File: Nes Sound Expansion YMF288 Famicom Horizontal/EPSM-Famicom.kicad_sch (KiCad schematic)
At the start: 67 parts, among them J1 CARTRIDGE_F, J2 CONSOLE_M, J3 AudioJack4_SwitchTR1, U1 74HC688, U10 74HC132, U11 74HC257, U12 74HC257, U13 LM358, U14 74LVC1G373, U15 74HC257, U2 74HC139, U3 74HC174, U4 74HC174, U5 74HC688, U6 74HC688, U7 74HC132, U8 YMF288, U9 BU9480F, X1 SG-8002CA

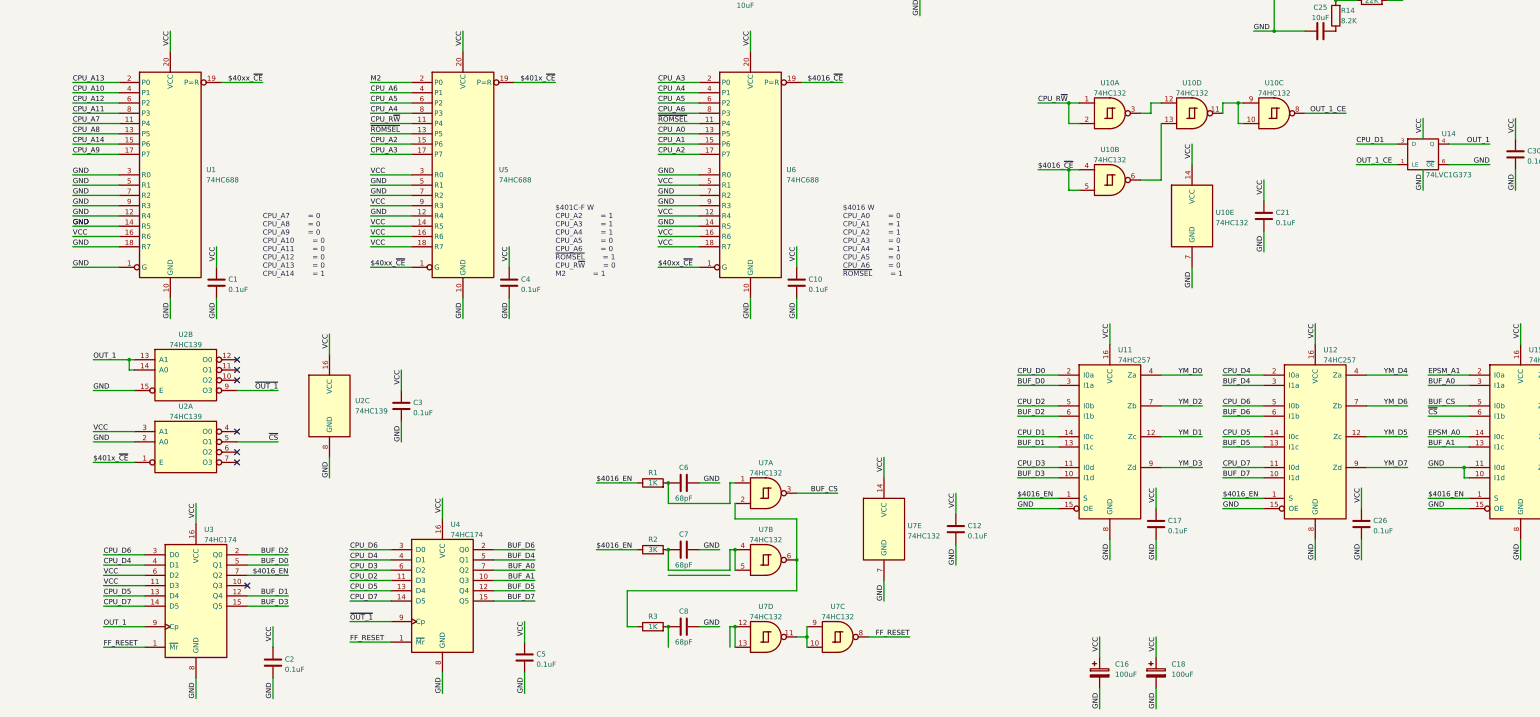
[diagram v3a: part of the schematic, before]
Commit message: Improved routing
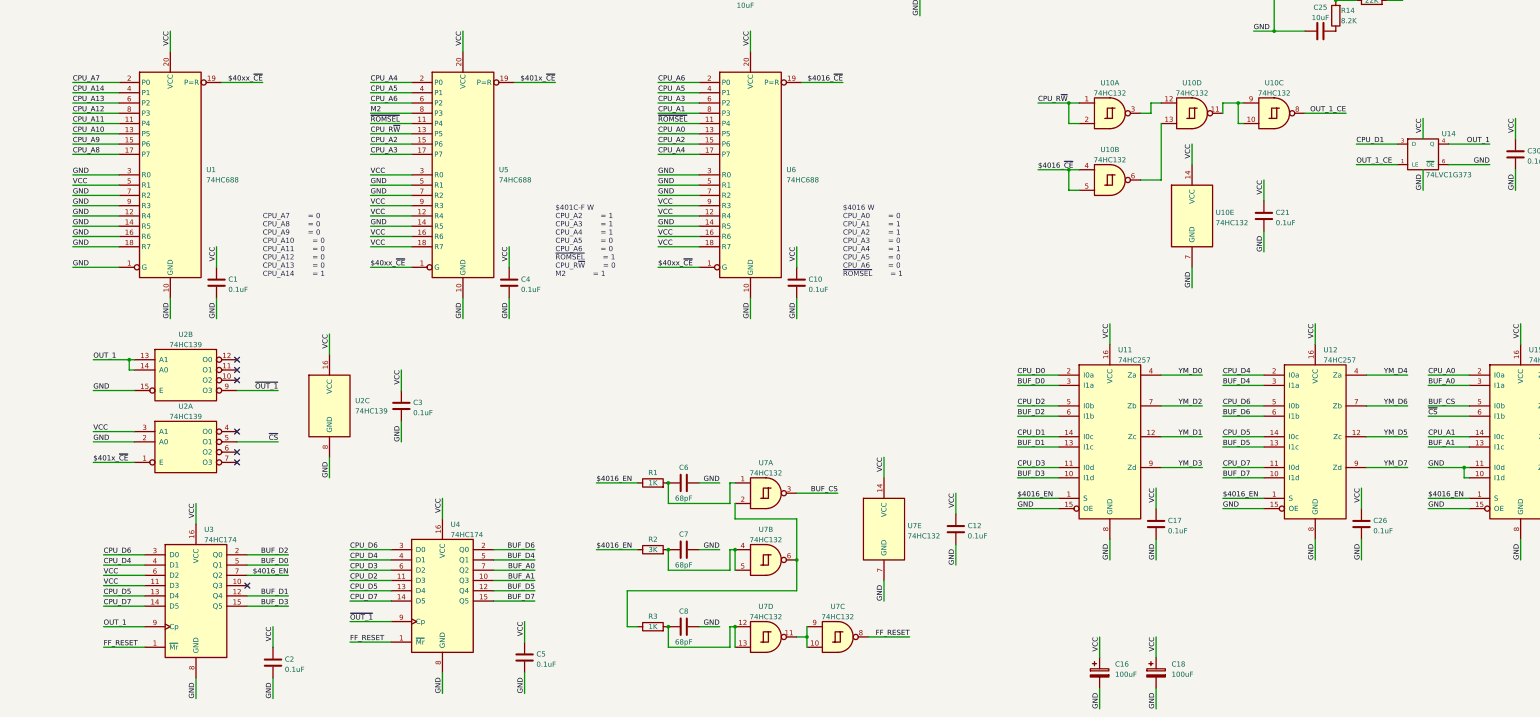
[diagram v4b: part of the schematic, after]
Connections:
- net EPSM_A0 is gone; now on net CPU_A1: U15.14 (I0c)
- net EPSM_A1 is gone; now on net CPU_A0: U15.2 (I0a)
- net CPU_A1: now also U6.8 (P3); no longer U6.15 (P6)
- net CPU_A10: now also U1.13 (P5); no longer U1.4 (P1)
- net CPU_A11: now also U1.11 (P4); no longer U1.8 (P3)
- net CPU_A12: now also U1.8 (P3); no longer U1.6 (P2)
- net CPU_A13: now also U1.6 (P2); no longer U1.2 (P0)
- net CPU_A14: now also U1.4 (P1); no longer U1.15 (P6)
- net CPU_A2: now also U6.15 (P6); no longer U6.17 (P7)
- net CPU_A3: now also U6.6 (P2); no longer U6.2 (P0)
- net CPU_A4: now also U5.2 (P0), U6.17 (P7); no longer U5.8 (P3), U6.4 (P1)
- net CPU_A5: now also U5.4 (P1), U6.4 (P1); no longer U5.6 (P2), U6.6 (P2)
- net CPU_A6: now also U5.6 (P2), U6.2 (P0); no longer U5.4 (P1), U6.8 (P3)
- net CPU_A7: now also U1.2 (P0); no longer U1.11 (P4)
- net CPU_A8: now also U1.17 (P7); no longer U1.13 (P5)
- net CPU_A9: now also U1.15 (P6); no longer U1.17 (P7)
- net CPU_R~{W}: now also U5.13 (P5); no longer U5.11 (P4)
- net GND: now also U1.16 (R6), U5.14 (R5), U6.5 (R1); no longer U1.5 (R1), U5.12 (R4), U6.9 (R3)
- net M2: now also U5.8 (P3); no longer U5.2 (P0)
- net VCC: now also U1.5 (R1), U5.12 (R4), U6.9 (R3); no longer U1.16 (R6), U5.14 (R5), U6.5 (R1)
- net ~{ROMSEL}: now also U5.11 (P4); no longer U5.13 (P5)
- net at U7.12, U7.13: now also C8.1, R3.2

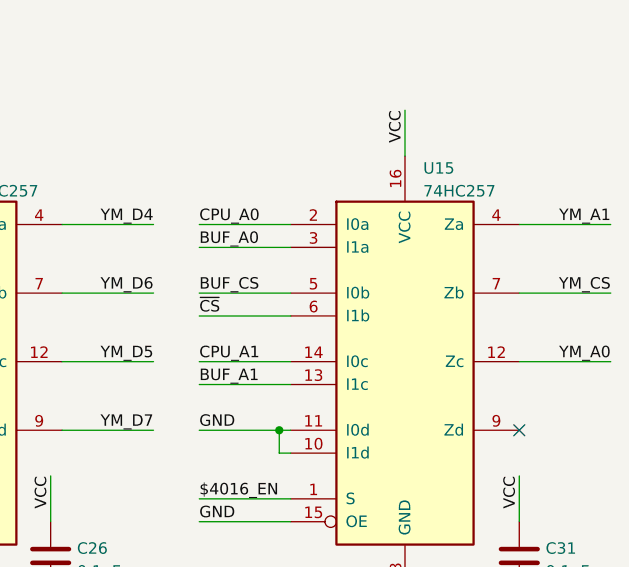
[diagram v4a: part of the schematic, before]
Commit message: Fix swapped connections
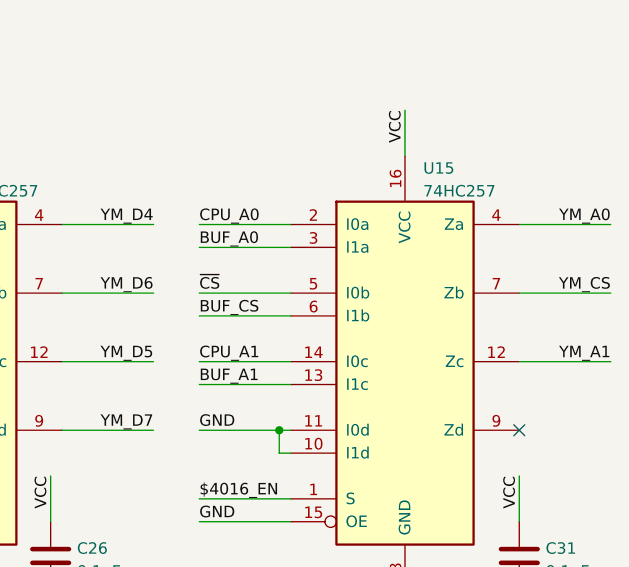
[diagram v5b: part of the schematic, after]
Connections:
- net BUF_CS: now also U15.6 (I1b); no longer U15.5 (I0b)
- net YM_A0: now also U15.4 (Za); no longer U15.12 (Zc)
- net YM_A1: now also U15.12 (Zc); no longer U15.4 (Za)
- net ~{CS}: now also U15.5 (I0b); no longer U15.6 (I1b)
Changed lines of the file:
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@@
   (title_block
     (title "EPSM Expansion Audio FC")
-    (date "2023-01-01")
-    (rev "B")
+    (date "2023-03-07")
+    (rev "B p.0.1.1")
     (company "Perkka; Persune")
   )
@@
     (effects (font (size 1.27 1.27)) (justify left bottom))
   )
-  (label "BUF_CS" (at 353.06 201.93 0)
+  (label "BUF_CS" (at 353.06 204.47 0)
     (effects (font (size 1.27 1.27)) (justify left bottom))
   )
@@
     (effects (font (size 1.27 1.27)) (justify left bottom))
   )
-  (label "YM_A1" (at 398.78 194.31 180)
+  (label "YM_A1" (at 398.78 209.55 180)
     (effects (font (size 1.27 1.27)) (justify right bottom))
   )
@@
     (effects (font (size 1.27 1.27)) (justify left bottom))
   )
-  (label "~{CS}" (at 353.06 204.47 0)
+  (label "~{CS}" (at 353.06 201.93 0)
     (effects (font (size 1.27 1.27)) (justify left bottom))
   )
@@
     (effects (font (size 1.27 1.27)) (justify right bottom))
   )
-  (label "YM_A0" (at 398.78 209.55 180)
-    (effects (font (size 1.27 1.27)) (justify right bottom))
-  )
+  (label "YM_A0" (at 398.78 194.31 180)
+    (effects (font (size 1.27 1.27)) (justify right bottom))
+  )
